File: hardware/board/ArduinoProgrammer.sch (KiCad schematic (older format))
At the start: 25 parts, among them J1 ISP_Programmer, J2 OLED_VCC-GND, J4 CONN_02X16, J5 CONN_01X02, J6 OLED_GND-VCC, SW1 SW_Push, SW2 SW_Push, U1 MIC5219-3.3BM5, U2 ATMEGA328-AU

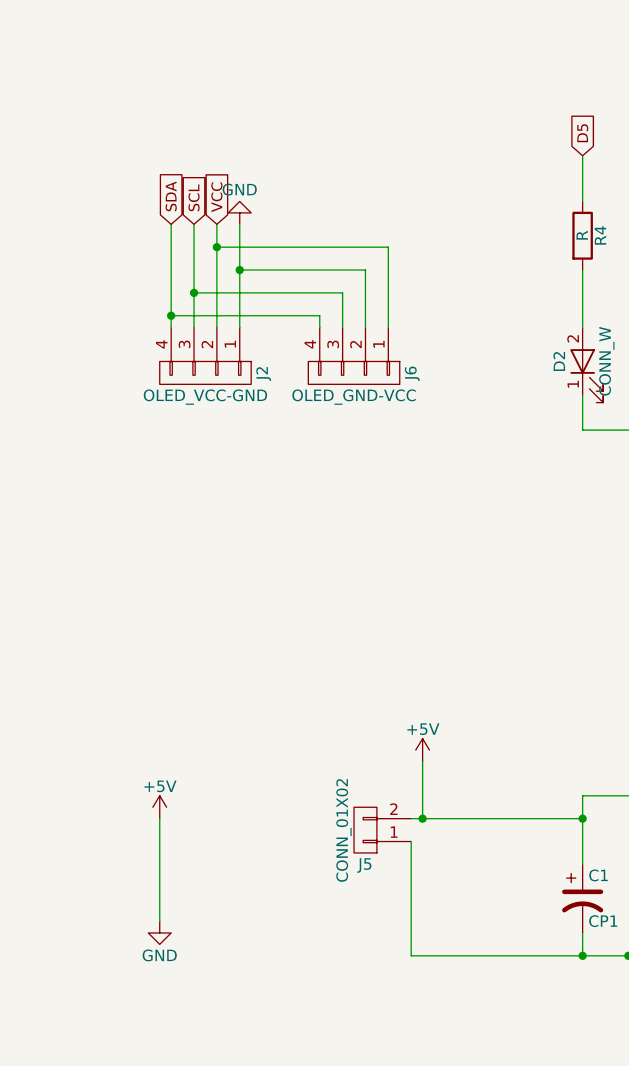
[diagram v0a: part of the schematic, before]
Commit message: Added pcb circuit with OSx auto-route
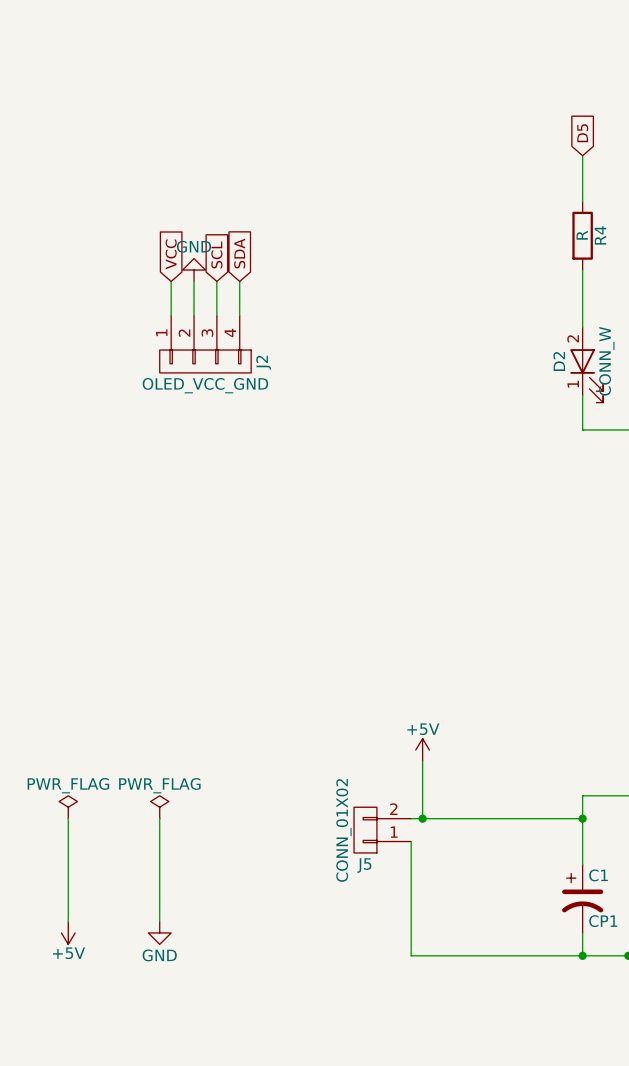
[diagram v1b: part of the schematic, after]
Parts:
- removed J2: OLED_VCC-GND, Pin_Headers:Pin_Header_Straight_1x04_Pitch2.00mm, symbol CONN_01X04
- removed J6: OLED_GND-VCC, Pin_Headers:Pin_Header_Straight_1x04_Pitch2.00mm, symbol CONN_01X04
- added J2: OLED_VCC_GND, AtMegaProgrammer:OLED_VCC_GND, symbol OLED_VCC_GND
- J4: footprint Pin_Headers:Pin_Header_Straight_2x16_Pitch2.00mm -> AtMegaProgrammer:ProgSocket
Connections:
- net +5V: no longer C1.2, C2.2, C3.2, C4.2, C6.2, D1.1 (K), D2.1 (K), D3.1 (K), D4.1 (K), J1.5 (P5), J1.6 (P6), J4.13 (P13), J5.1 (P1), R2.2, SW1.2, U1.2 (GND), U2.21 (GND), U2.3 (GND), U2.5 (GND)
- net SCL: now also J2.3 (SCL)
- net SDA: now also J2.4 (SDA)
- net VCC: now also J2.1 (VCC)
- new net GND: C1.2, C2.2, C3.2, C4.2, C6.2, D1.1 (K), D2.1 (K), D3.1 (K), D4.1 (K), J1.5 (P5), J1.6 (P6), J2.2 (GND), J4.13 (P13), J5.1 (P1), R2.2, SW1.2, U1.2 (GND), U2.21 (GND), U2.3 (GND), U2.5 (GND)
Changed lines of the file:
@@
 LIBS:valves
 LIBS:switches
+LIBS:AtMegaProgramerParts
 LIBS:ArduinoProgrammer-cache
 EELAYER 25 0
@@
 F 0 "J4" H 2500 2500 50  0000 C CNN
 F 1 "CONN_02X16" V 2500 1650 50  0000 C CNN
-F 2 "Pin_Headers:Pin_Header_Straight_2x16_Pitch2.00mm" H 2500 550 50  0001 C CNN
+F 2 "AtMegaProgrammer:ProgSocket" H 2500 550 50  0001 C CNN
 F 3 "" H 2500 550 50  0001 C CNN
 	1    2500 1650
@@
 $EndComp
 $Comp
-L CONN_01X04 J2
-U 1 1 59BA0C0D
-P 1350 4600
-F 0 "J2" H 1350 4850 50  0000 C CNN
-F 1 "OLED_VCC-GND" V 1450 4600 50  0000 C CNN
-F 2 "Pin_Headers:Pin_Header_Straight_1x04_Pitch2.00mm" H 1350 4600 50  0001 C CNN
-F 3 "" H 1350 4600 50  0001 C CNN
-	1    1350 4600
-	0    1    1    0
-$EndComp
-$Comp
 L GND #PWR09
 U 1 1 59BA13D2
-P 1500 3950
-F 0 "#PWR09" H 1500 3700 50  0001 C CNN
-F 1 "GND" H 1500 3800 50  0000 C CNN
-F 2 "" H 1500 3950 50  0001 C CNN
-F 3 "" H 1500 3950 50  0001 C CNN
-	1    1500 3950
+P 1300 4200
+F 0 "#PWR09" H 1300 3950 50  0001 C CNN
+F 1 "GND" H 1300 4050 50  0000 C CNN
+F 2 "" H 1300 4200 50  0001 C CNN
+F 3 "" H 1300 4200 50  0001 C CNN
+	1    1300 4200
 	-1   0    0    1
 $EndComp
-Text GLabel 1400 3950 1    47   Input ~ 0
+Text GLabel 1200 4200 1    47   Input ~ 0
 VCC
-Text GLabel 1300 3950 1    47   Input ~ 0
+Text GLabel 1400 4200 1    47   Input ~ 0
 SCL
-Text GLabel 1200 3950 1    47   Input ~ 0
+Text GLabel 1500 4200 1    47   Input ~ 0
 SDA
 Text GLabel 7050 3100 2    47   Input ~ 0
@@
 Text GLabel 7100 2350 2    47   Input ~ 0
 P_SCK
-$Comp
-L CONN_01X04 J6
-U 1 1 59C6E50B
-P 2000 4600
-F 0 "J6" H 2000 4850 50  0000 C CNN
-F 1 "OLED_GND-VCC" V 2100 4600 50  0000 C CNN
-F 2 "Pin_Headers:Pin_Header_Straight_1x04_Pitch2.00mm" H 2000 4600 50  0001 C CNN
-F 3 "" H 2000 4600 50  0001 C CNN
-	1    2000 4600
-	0    1    1    0
-$EndComp
 Wire Wire Line
 	4300 6450 5500 6450
@@
 Connection ~ 5000 7150
 Wire Wire Line
-	1200 3950 1200 4400
-Wire Wire Line
-	1300 3950 1300 4400
-Wire Wire Line
-	1400 3950 1400 4400
-Wire Wire Line
-	1500 3950 1500 4400
-Wire Wire Line
 	7050 3100 6850 3100
 Wire Wire Line
@@
 Wire Wire Line
 	7100 2350 6850 2350
-Wire Wire Line
-	1200 4350 1850 4350
-Wire Wire Line
-	1850 4350 1850 4400
-Connection ~ 1200 4350
-Wire Wire Line
-	1950 4400 1950 4250
-Wire Wire Line
-	1950 4250 1300 4250
-Connection ~ 1300 4250
-Wire Wire Line
-	2050 4400 2050 4150
-Wire Wire Line
-	2050 4150 1500 4150
-Connection ~ 1500 4150
-Wire Wire Line
-	1400 4050 2150 4050
-Wire Wire Line
-	2150 4050 2150 4400
-Connection ~ 1400 4050
 $Comp
 L R R4
@@
 	1    0    0    -1
 $EndComp
-$Comp
-L +5V #PWR012
-U 1 1 59CCAA13
+Wire Wire Line
+	1150 6550 1150 7000
+NoConn ~ 4300 6650
+$Comp
+L PWR_FLAG #FLG012
+U 1 1 59D3EC00
 P 1150 6550
-F 0 "#PWR012" H 1150 6400 50  0001 C CNN
-F 1 "+5V" H 1150 6690 50  0000 C CNN
+F 0 "#FLG012" H 1150 6625 50  0001 C CNN
+F 1 "PWR_FLAG" H 1150 6700 50  0000 C CNN
 F 2 "" H 1150 6550 50  0001 C CNN
 F 3 "" H 1150 6550 50  0001 C CNN
@@
 	1    0    0    -1
 $EndComp
-Wire Wire Line
-	1150 6550 1150 7000
-NoConn ~ 4300 6650
+$Comp
+L PWR_FLAG #FLG013
+U 1 1 59D3EE44
+P 750 6550
+F 0 "#FLG013" H 750 6625 50  0001 C CNN
+F 1 "PWR_FLAG" H 750 6700 50  0000 C CNN
+F 2 "" H 750 6550 50  0001 C CNN
+F 3 "" H 750 6550 50  0001 C CNN
+	1    750  6550
+	1    0    0    -1
+$EndComp
+$Comp
+L +5V #PWR014
+U 1 1 59D3EEA3
+P 750 7000
+F 0 "#PWR014" H 750 6850 50  0001 C CNN
+F 1 "+5V" H 750 7140 50  0000 C CNN
+F 2 "" H 750 7000 50  0001 C CNN
+F 3 "" H 750 7000 50  0001 C CNN
+	1    750  7000
+	-1   0    0    1
+$EndComp
+Wire Wire Line
+	750  6550 750  7000
+$Comp
+L OLED_VCC_GND J2
+U 1 1 59D5807D
+P 1350 4550
+F 0 "J2" V 1600 4550 50  0000 C CNN
+F 1 "OLED_VCC_GND" H 1350 4450 50  0000 C CNN
+F 2 "AtMegaProgrammer:OLED_VCC_GND" V 1350 4550 50  0001 C CNN
+F 3 "" V 1350 4550 50  0001 C CNN
+	1    1350 4550
+	1    0    0    -1
+$EndComp
+Wire Wire Line
+	1200 4200 1200 4350
+Wire Wire Line
+	1300 4200 1300 4350
+Wire Wire Line
+	1400 4200 1400 4350
+Wire Wire Line
+	1500 4200 1500 4350
 $EndSCHEMATC
